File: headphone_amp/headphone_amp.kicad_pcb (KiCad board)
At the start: 2 copper layers, 100 x 50 mm, 40 parts, among them J1 Molex_SL_01x02_Male, J2 Molex_SL_01x02_Male, J3 Molex_SL_01x03_Male, J4 Molex_SL_01x03_Male, Q1 PZTA42, Q2 PZTA92, Q3 PZTA42, Q4 PZTA92, U1 NE5532

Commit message: update output cap footprint and bleeder resistor
- update output cap footprint (20mm height vs 25mm to match actual part)
- increase bleeder resistor value to 22k from 10k, to decrease corner
frequency
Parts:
- C3, C6: footprint Capacitor_THT:C_Radial_D12.5mm_H25.0mm_P5.00mm -> Capacitor_THT:C_Radial_D12.5mm_H20.0mm_P5.00mm
- R16, R8: value 10k -> 22k
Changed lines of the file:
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@@
     (add_net VEE)
+  )
+  (module Capacitor_THT:C_Radial_D12.5mm_H20.0mm_P5.00mm (layer F.Cu)
+    (at 169 124 180)
+    (descr "C, Radial series, Radial, pin pitch=5.00mm, diameter=12.5mm, height=20mm, Non-Polar Electrolytic Capacitor")
+    (tags "C Radial series Radial pin pitch 5.00mm diameter 12.5mm height 20mm Non-Polar Electrolytic Capacitor")
+    (fp_text reference C6 (at 2.5 -7.5) (layer F.SilkS)
+      (effects (font (size 1 1) (thickness 0.15)))
+    )
+    (fp_text value 220u (at 2.5 7.5) (layer F.Fab)
+      (effects (font (size 1 1) (thickness 0.15)))
+    )
+    (fp_text user %R (at 2.5 0) (layer F.Fab)
+      (effects (font (size 1 1) (thickness 0.15)))
+    )
+    (fp_circle (center 2.5 0) (end 9 0) (layer F.CrtYd) (width 0.05))
+    (fp_circle (center 2.5 0) (end 8.87 0) (layer F.SilkS) (width 0.12))
+    (fp_circle (center 2.5 0) (end 8.75 0) (layer F.Fab) (width 0.1))
+    (pad 2 thru_hole circle (at 5 0 180) (size 1.6 1.6) (drill 0.8) (layers *.Cu *.Mask)
+      (net 6 "Net-(C4-Pad1)"))
+    (pad 1 thru_hole circle (at 0 0 180) (size 1.6 1.6) (drill 0.8) (layers *.Cu *.Mask)
+      (net 20 /right_out))
+    (model ${KISYS3DMOD}/Capacitor_THT.3dshapes/C_Radial_D12.5mm_H20.0mm_P5.00mm.wrl
+      (at (xyz 0 0 0))
+      (scale (xyz 1 1 1))
+      (rotate (xyz 0 0 0))
+    )
+  )
+  (module Capacitor_THT:C_Radial_D12.5mm_H20.0mm_P5.00mm (layer F.Cu)
+    (at 169 110.5 180)
+    (descr "C, Radial series, Radial, pin pitch=5.00mm, diameter=12.5mm, height=20mm, Non-Polar Electrolytic Capacitor")
+    (tags "C Radial series Radial pin pitch 5.00mm diameter 12.5mm height 20mm Non-Polar Electrolytic Capacitor")
+    (fp_text reference C3 (at 2.5 -7.5) (layer F.SilkS)
+      (effects (font (size 1 1) (thickness 0.15)))
+    )
+    (fp_text value 220u (at 2.5 7.5) (layer F.Fab)
+      (effects (font (size 1 1) (thickness 0.15)))
+    )
+    (fp_text user %R (at 2.5 0) (layer F.Fab)
+      (effects (font (size 1 1) (thickness 0.15)))
+    )
+    (fp_circle (center 2.5 0) (end 9 0) (layer F.CrtYd) (width 0.05))
+    (fp_circle (center 2.5 0) (end 8.87 0) (layer F.SilkS) (width 0.12))
+    (fp_circle (center 2.5 0) (end 8.75 0) (layer F.Fab) (width 0.1))
+    (pad 2 thru_hole circle (at 5 0 180) (size 1.6 1.6) (drill 0.8) (layers *.Cu *.Mask)
+      (net 2 "Net-(C1-Pad1)"))
+    (pad 1 thru_hole circle (at 0 0 180) (size 1.6 1.6) (drill 0.8) (layers *.Cu *.Mask)
+      (net 21 /left_out))
+    (model ${KISYS3DMOD}/Capacitor_THT.3dshapes/C_Radial_D12.5mm_H20.0mm_P5.00mm.wrl
+      (at (xyz 0 0 0))
+      (scale (xyz 1 1 1))
+      (rotate (xyz 0 0 0))
+    )
   )
   (module Resistor_SMD:R_0603_1608Metric_Pad1.05x0.95mm_HandSolder (layer F.Cu)
@@
       (effects (font (size 1 1) (thickness 0.15)))
     )
-    (fp_text value 10k (at 0 1.43 90) (layer F.Fab)
+    (fp_text value 22k (at 0 1.43 90) (layer F.Fab)
       (effects (font (size 1 1) (thickness 0.15)))
     )
@@
       (effects (font (size 1 1) (thickness 0.15)))
     )
-    (fp_text value 10k (at 0 1.43 90) (layer F.Fab)
+    (fp_text value 22k (at 0 1.43 90) (layer F.Fab)
       (effects (font (size 1 1) (thickness 0.15)))
     )
@@
     )
   )
-  (module Capacitor_THT:C_Radial_D12.5mm_H25.0mm_P5.00mm (layer F.Cu)
-    (at 169 124 180)
-    (descr "C, Radial series, Radial, pin pitch=5.00mm, diameter=12.5mm, height=25mm, Non-Polar Electrolytic Capacitor")
-    (tags "C Radial series Radial pin pitch 5.00mm diameter 12.5mm height 25mm Non-Polar Electrolytic Capacitor")
-    (fp_text reference C6 (at 2.5 -7.5) (layer F.SilkS)
-      (effects (font (size 1 1) (thickness 0.15)))
-    )
-    (fp_text value 220u (at 2.5 7.5) (layer F.Fab)
-      (effects (font (size 1 1) (thickness 0.15)))
-    )
-    (fp_text user %R (at 2.5 0) (layer F.Fab)
-      (effects (font (size 1 1) (thickness 0.15)))
-    )
-    (fp_circle (center 2.5 0) (end 9 0) (layer F.CrtYd) (width 0.05))
-    (fp_circle (center 2.5 0) (end 8.87 0) (layer F.SilkS) (width 0.12))
-    (fp_circle (center 2.5 0) (end 8.75 0) (layer F.Fab) (width 0.1))
-    (pad 2 thru_hole circle (at 5 0 180) (size 1.6 1.6) (drill 0.8) (layers *.Cu *.Mask)
-      (net 6 "Net-(C4-Pad1)"))
-    (pad 1 thru_hole circle (at 0 0 180) (size 1.6 1.6) (drill 0.8) (layers *.Cu *.Mask)
-      (net 20 /right_out))
-    (model ${KISYS3DMOD}/Capacitor_THT.3dshapes/C_Radial_D12.5mm_H25.0mm_P5.00mm.wrl
-      (at (xyz 0 0 0))
-      (scale (xyz 1 1 1))
-      (rotate (xyz 0 0 0))
-    )
-  )
   (module Capacitor_SMD:C_0603_1608Metric_Pad1.05x0.95mm_HandSolder (layer F.Cu)
     (at 124.816 125.516 270)
@@
       (at (xyz 0 0 0))
       (scale (xyz 1 1 1))
-      (rotate (xyz 0 0 0))
-    )
-  )
-  (module Capacitor_THT:C_Radial_D12.5mm_H25.0mm_P5.00mm (layer F.Cu)
-    (at 169 110.5 180)
-    (descr "C, Radial series, Radial, pin pitch=5.00mm, diameter=12.5mm, height=25mm, Non-Polar Electrolytic Capacitor")
-    (tags "C Radial series Radial pin pitch 5.00mm diameter 12.5mm height 25mm Non-Polar Electrolytic Capacitor")
-    (fp_text reference C3 (at 2.5 -7.5) (layer F.SilkS)
-      (effects (font (size 1 1) (thickness 0.15)))
-    )
-    (fp_text value 220u (at 2.5 7.5) (layer F.Fab)
-      (effects (font (size 1 1) (thickness 0.15)))
-    )
-    (fp_circle (center 2.5 0) (end 8.75 0) (layer F.Fab) (width 0.1))
-    (fp_circle (center 2.5 0) (end 8.87 0) (layer F.SilkS) (width 0.12))
-    (fp_circle (center 2.5 0) (end 9 0) (layer F.CrtYd) (width 0.05))
-    (fp_text user %R (at 2.5 0) (layer F.Fab)
-      (effects (font (size 1 1) (thickness 0.15)))
-    )
-    (pad 1 thru_hole circle (at 0 0 180) (size 1.6 1.6) (drill 0.8) (layers *.Cu *.Mask)
-      (net 21 /left_out))
-    (pad 2 thru_hole circle (at 5 0 180) (size 1.6 1.6) (drill 0.8) (layers *.Cu *.Mask)
-      (net 2 "Net-(C1-Pad1)"))
-    (model ${KISYS3DMOD}/Capacitor_THT.3dshapes/C_Radial_D12.5mm_H25.0mm_P5.00mm.wrl
-      (at (xyz 0 0 0))
-      (scale (xyz 1 1 1))

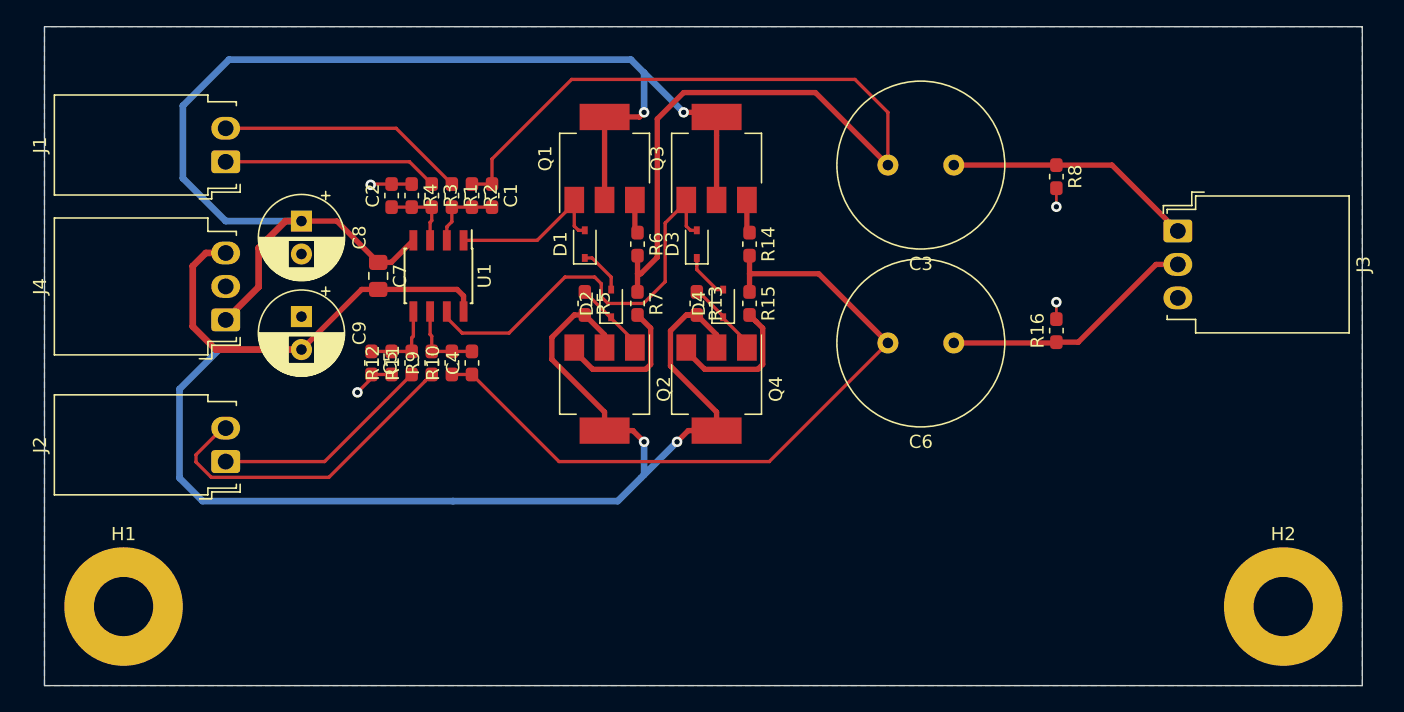
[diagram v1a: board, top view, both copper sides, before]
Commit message: clean up fab labels and silkscreen
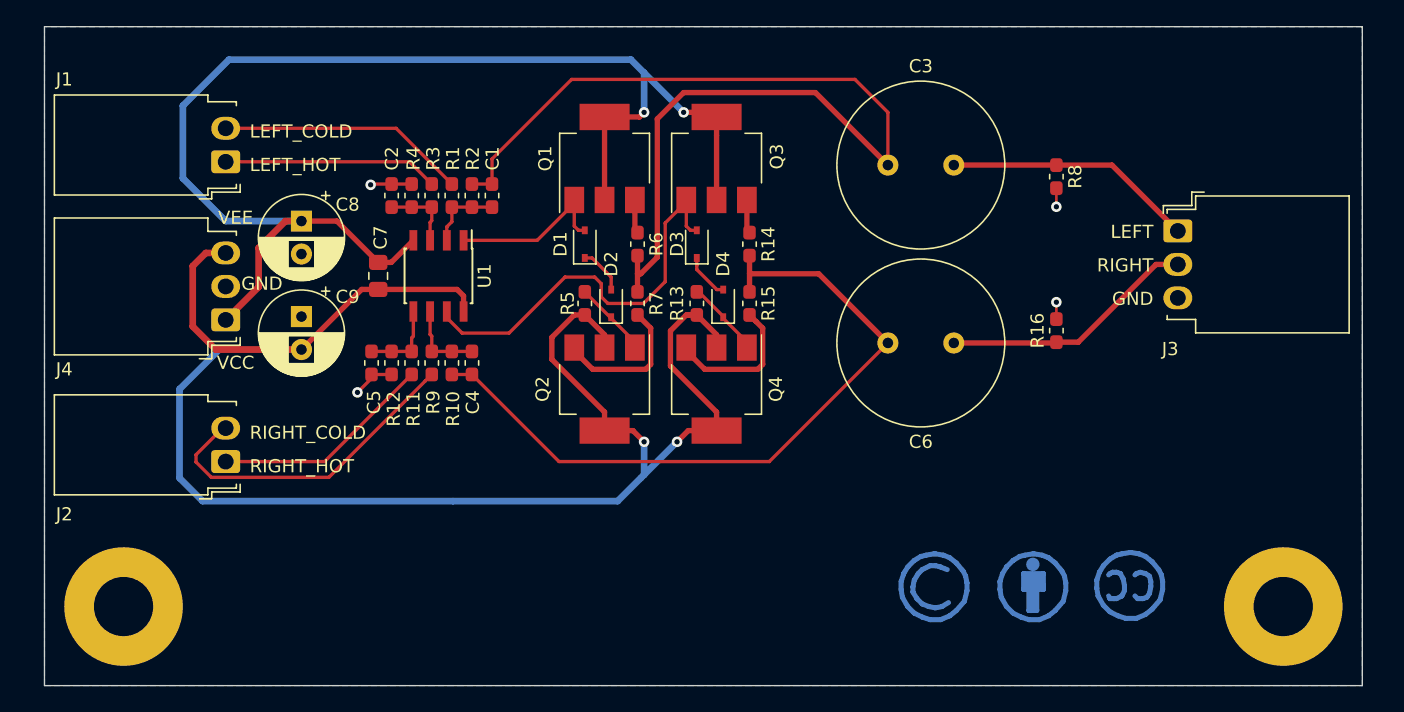
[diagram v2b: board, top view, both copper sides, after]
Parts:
- added REF**: Symbol_CC-Attribution_CopperTop_Small, Symbol:Symbol_CC-Attribution_CopperTop_Small, B.Cu at (175.0, 142.5)
- added REF**: Symbol_CC-ShareAlike_CopperTop_Small, Symbol:Symbol_CC-ShareAlike_CopperTop_Small, B.Cu at (167.5, 142.5)
- added REF**: Symbol_CreativeCommons_CopperTop_Type2_Small, Symbol:Symbol_CreativeCommons_CopperTop_Type2_Small, B.Cu at (182.5, 142.5)
- added REF**: OSHW-Logo2_9.8x8mm_SilkScreen, Symbol:OSHW-Logo2_9.8x8mm_SilkScreen, B.Cu at (140.0, 142.5)
- added REF**: KiCad-Logo2_8mm_SilkScreen, Symbol:KiCad-Logo2_8mm_SilkScreen, B.Cu at (125.0, 142.5)
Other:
- board text added: "https://creativecommons.org/licenses/by-sa/4.0/"

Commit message: connect output jack ground to star point with net tie
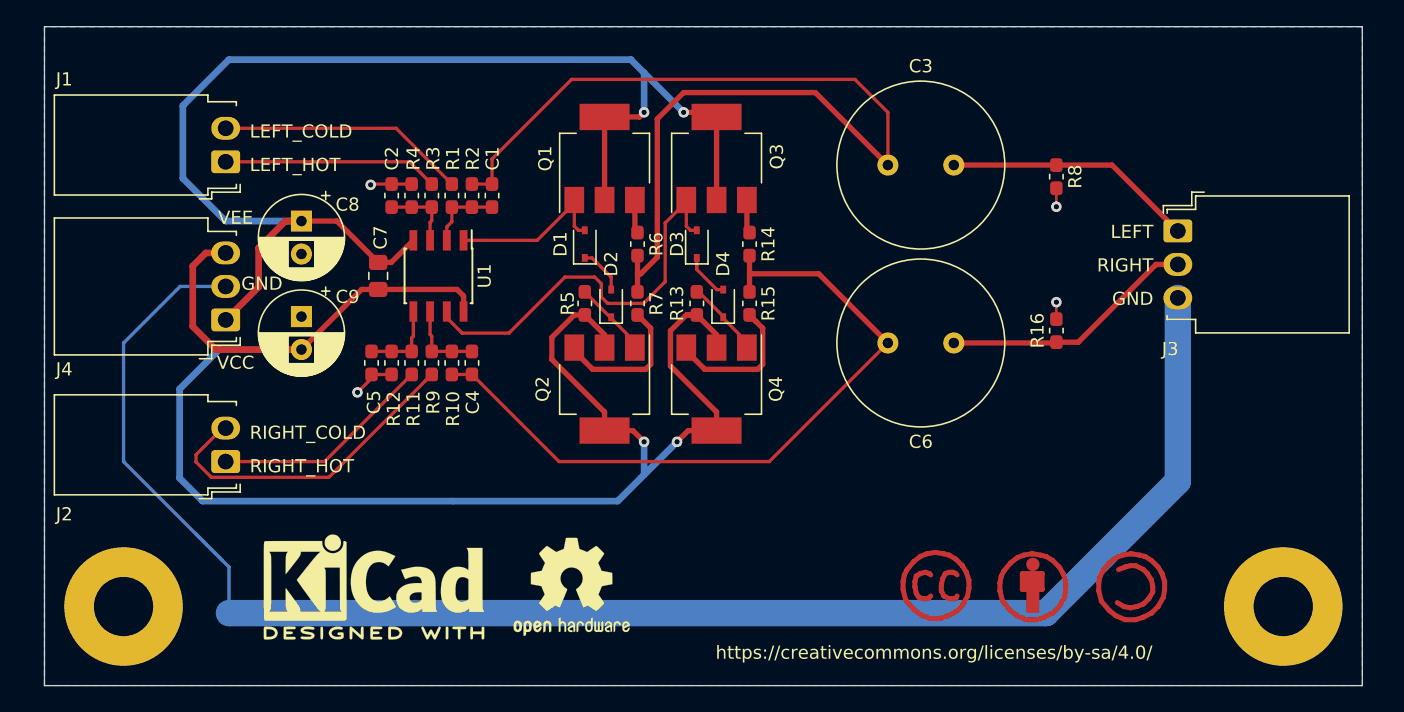
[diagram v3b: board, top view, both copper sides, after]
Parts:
- added NT1: Net-Tie_2, NetTie:NetTie-2_SMD_Pad2.0mm, B.Cu at (116.0, 144.5)
- REF** (x5): moved to F.Cu
- moved REF** 15.0 mm to (182.5, 142.5), turned to 0 degrees
- moved REF** 15.0 mm to (167.5, 142.5), turned to 0 degrees
- turned REF** to 0 degrees (x3)
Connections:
- J3 pad 3: GNDA -> /gnd_out
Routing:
- net /gnd_out: track 0.00 -> 86.1 mm
- net GNDA: track 9.16 -> 45.3 mm
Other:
- board text added: "TODO check height of all components, especially output caps choose orientation and rearrange connectors?"
- board text removed: "TODO check height of all components, especially output caps choose orientation and rearrange connectors? connect output ground to star ground add kicad/oshw/CC BY-SA labels"

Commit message: add info silk to headphone amplifier
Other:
- board text added: "Headphone Amplifier Board rev0 Preamp 2019 G. Keeth 2019-09-22"
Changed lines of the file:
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@@
   (general
     (thickness 1.6)
-    (drawings 9)
+    (drawings 10)
     (tracks 211)
     (zones 0)
@@
     )
   )
+  (gr_text "Headphone Amplifier Board rev0\nPreamp 2019\nG. Keeth\n2019-09-22" (at 199 104) (layer B.SilkS)
+    (effects (font (size 1 1) (thickness 0.15)) (justify left mirror))
+  )
   (gr_text https://creativecommons.org/licenses/by-sa/4.0/ (at 167.5 147.5) (layer F.SilkS)

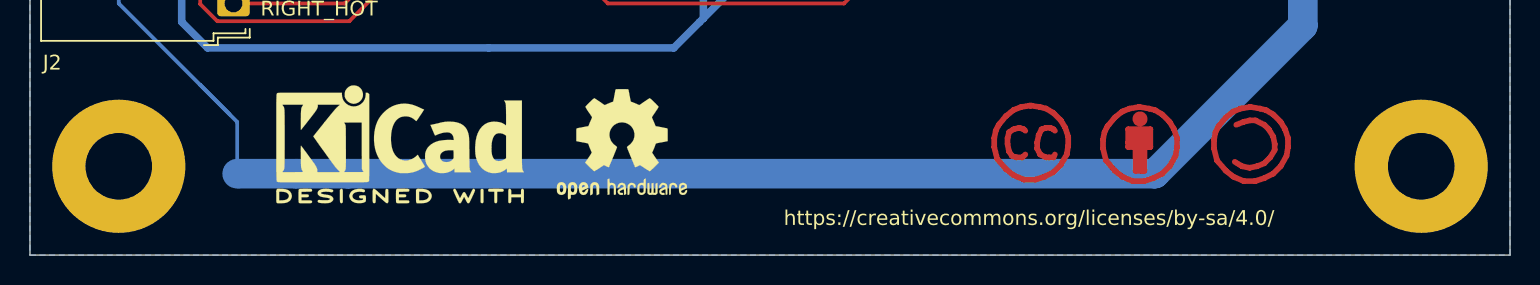
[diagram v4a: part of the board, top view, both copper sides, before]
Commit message: change to M3 mounting holes
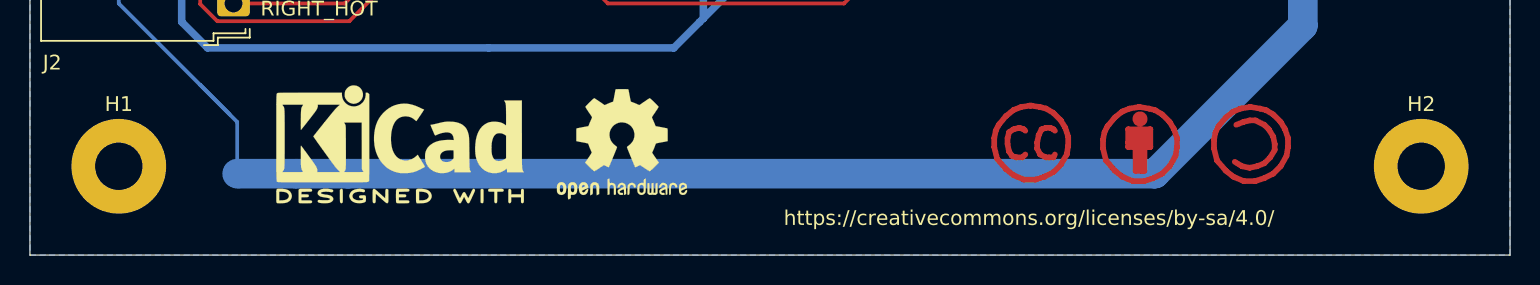
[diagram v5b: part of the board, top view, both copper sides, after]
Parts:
- H1, H2: footprint MountingHole:MountingHole_4.5mm_Pad -> MountingHole:MountingHole_3.2mm_M3_Pad
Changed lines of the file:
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@@
     (add_net VEE)
+  )
+  (module MountingHole:MountingHole_3.2mm_M3_Pad (layer F.Cu)
+    (at 194 144)
+    (descr "Mounting Hole 3.2mm, M3")
+    (tags "mounting hole 3.2mm m3")
+    (attr virtual)
+    (fp_text reference H2 (at 0 -4.2) (layer F.SilkS)
+      (effects (font (size 1 1) (thickness 0.15)))
+    )
+    (fp_text value MountingHole_Pad (at 0 4.2) (layer F.Fab)
+      (effects (font (size 1 1) (thickness 0.15)))
+    )
+    (fp_circle (center 0 0) (end 3.45 0) (layer F.CrtYd) (width 0.05))
+    (fp_circle (center 0 0) (end 3.2 0) (layer Cmts.User) (width 0.15))
+    (fp_text user %R (at 0.3 0) (layer F.Fab)
+      (effects (font (size 1 1) (thickness 0.15)))
+    )
+    (pad 1 thru_hole circle (at 0 0) (size 6.4 6.4) (drill 3.2) (layers *.Cu *.Mask)
+      (net 3 GNDA))
+  )
+  (module MountingHole:MountingHole_3.2mm_M3_Pad (layer F.Cu)
+    (at 106 144)
+    (descr "Mounting Hole 3.2mm, M3")
+    (tags "mounting hole 3.2mm m3")
+    (attr virtual)
+    (fp_text reference H1 (at 0 -4.2) (layer F.SilkS)
+      (effects (font (size 1 1) (thickness 0.15)))
+    )
+    (fp_text value MountingHole_Pad (at 0 4.2) (layer F.Fab)
+      (effects (font (size 1 1) (thickness 0.15)))
+    )
+    (fp_circle (center 0 0) (end 3.45 0) (layer F.CrtYd) (width 0.05))
+    (fp_circle (center 0 0) (end 3.2 0) (layer Cmts.User) (width 0.15))
+    (fp_text user %R (at 0.3 0) (layer F.Fab)
+      (effects (font (size 1 1) (thickness 0.15)))
+    )
+    (pad 1 thru_hole circle (at 0 0) (size 6.4 6.4) (drill 3.2) (layers *.Cu *.Mask)
+      (net 3 GNDA))
   )
   (module NetTie:NetTie-2_SMD_Pad2.0mm (layer B.Cu)
@@
     )
   )
-  (module MountingHole:MountingHole_4.5mm_Pad (layer F.Cu)
-    (at 194 144)
-    (descr "Mounting Hole 4.5mm")
-    (tags "mounting hole 4.5mm")
-    (attr virtual)
-    (fp_text reference H2 (at 0 -5.5) (layer F.SilkS) hide
-      (effects (font (size 1 1) (thickness 0.15)))
-    )
-    (fp_text value MountingHole_Pad (at 0 5.5) (layer F.Fab)
-      (effects (font (size 1 1) (thickness 0.15)))
-    )
-    (fp_circle (center 0 0) (end 4.75 0) (layer F.CrtYd) (width 0.05))
-    (fp_circle (center 0 0) (end 4.5 0) (layer Cmts.User) (width 0.15))
-    (fp_text user %R (at 0.3 0) (layer F.Fab)
-      (effects (font (size 1 1) (thickness 0.15)))
-    )
-    (pad 1 thru_hole circle (at 0 0) (size 9 9) (drill 4.5) (layers *.Cu *.Mask)
-      (net 3 GNDA))
-  )
-  (module MountingHole:MountingHole_4.5mm_Pad (layer F.Cu)
-    (at 106 144)
-    (descr "Mounting Hole 4.5mm")
-    (tags "mounting hole 4.5mm")
-    (attr virtual)
-    (fp_text reference H1 (at 0 -5.5) (layer F.SilkS) hide
-      (effects (font (size 1 1) (thickness 0.15)))
-    )
-    (fp_text value MountingHole_Pad (at 0 5.5) (layer F.Fab)
-      (effects (font (size 1 1) (thickness 0.15)))
-    )
-    (fp_circle (center 0 0) (end 4.75 0) (layer F.CrtYd) (width 0.05))
-    (fp_circle (center 0 0) (end 4.5 0) (layer Cmts.User) (width 0.15))
-    (fp_text user %R (at 0.3 0) (layer F.Fab)
-      (effects (font (size 1 1) (thickness 0.15)))
-    )
-    (pad 1 thru_hole circle (at 0 0) (size 9 9) (drill 4.5) (layers *.Cu *.Mask)
-      (net 3 GNDA))
-  )
   (module Diode_SMD:D_SOD-323 (layer F.Cu)

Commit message: update TODO list with chassis mount jack
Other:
- board text added: "TODO check height of all components, especially output caps choose orientation and rearrange connectors? chassis mount jack?"
- board text removed: "TODO check height of all components, especially output caps choose orientation and rearrange connectors?"
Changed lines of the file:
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@@
     (arrow2b (pts (xy 89 150) (xy 88.413579 148.873496)))
   )
-  (gr_text "TODO\ncheck height of all components, especially output caps\nchoose orientation and rearrange connectors?" (at 128.5 92) (layer Cmts.User)
+  (gr_text "TODO\ncheck height of all components, especially output caps\nchoose orientation and rearrange connectors?\nchassis mount jack?" (at 128.5 92) (layer Cmts.User)
     (effects (font (size 1.5 1.5) (thickness 0.3)) (justify left))
   )
